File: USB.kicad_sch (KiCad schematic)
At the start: 44 parts, among them J2 24FLZ-SM2-TB, J5 DM3BT-DSF-PEJS, M1 IMP34DT05TR, M2 IMP34DT05TR, Q1 AO3401A, U3 FDS9926A

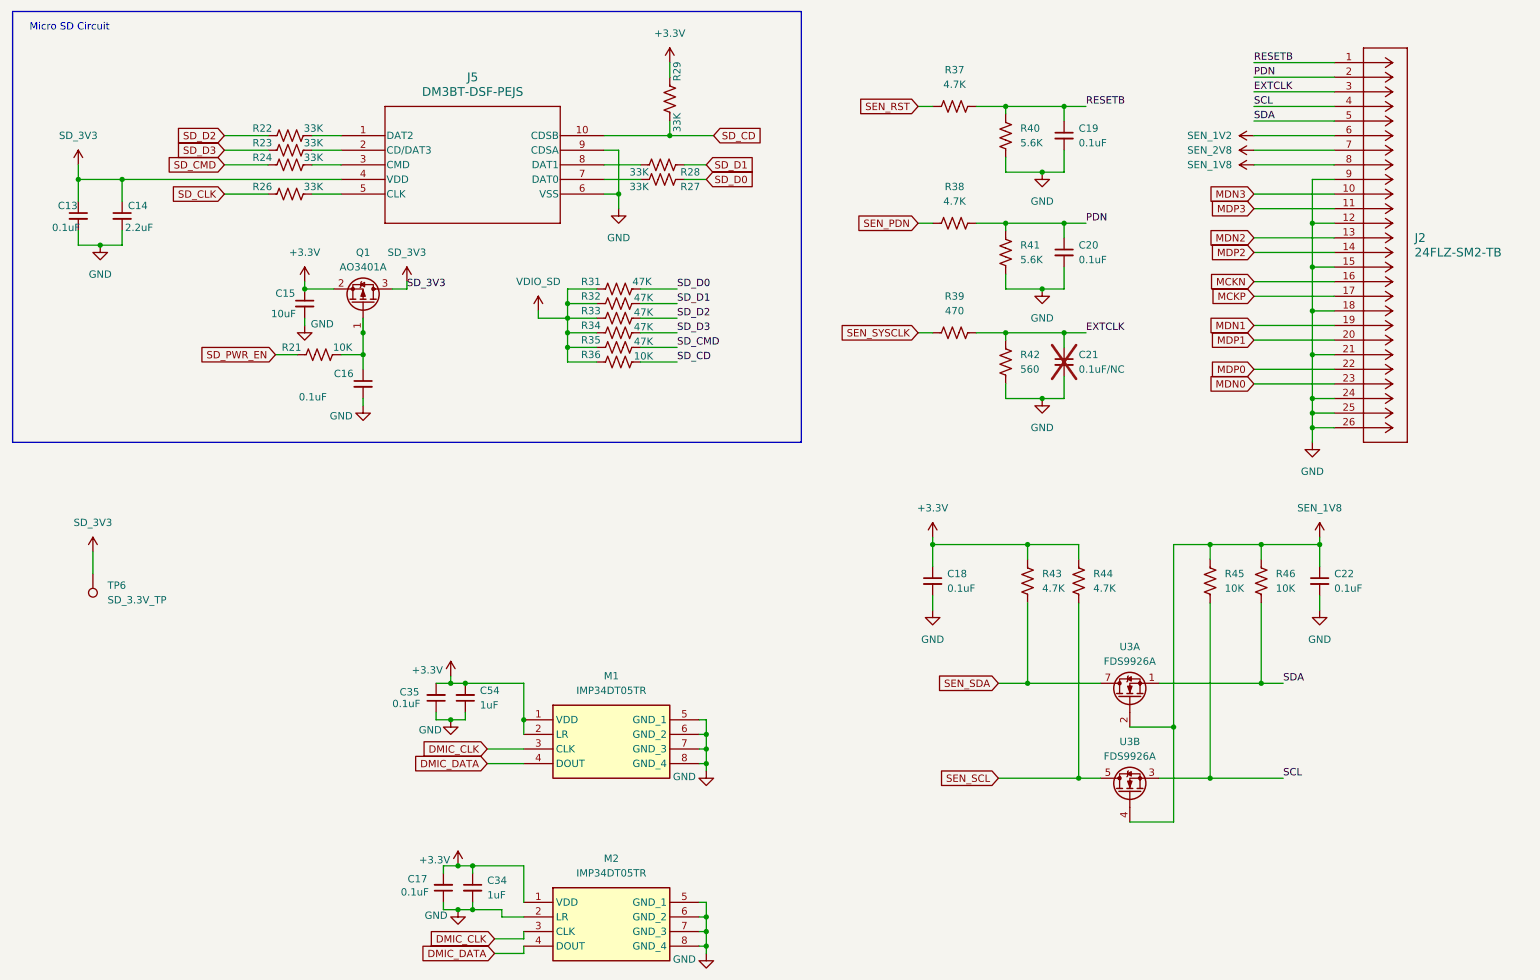
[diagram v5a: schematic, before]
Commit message: Replaced all passive footprints from 0603 metric to 0603 imperial. Big oversight. All done. Next is DRC
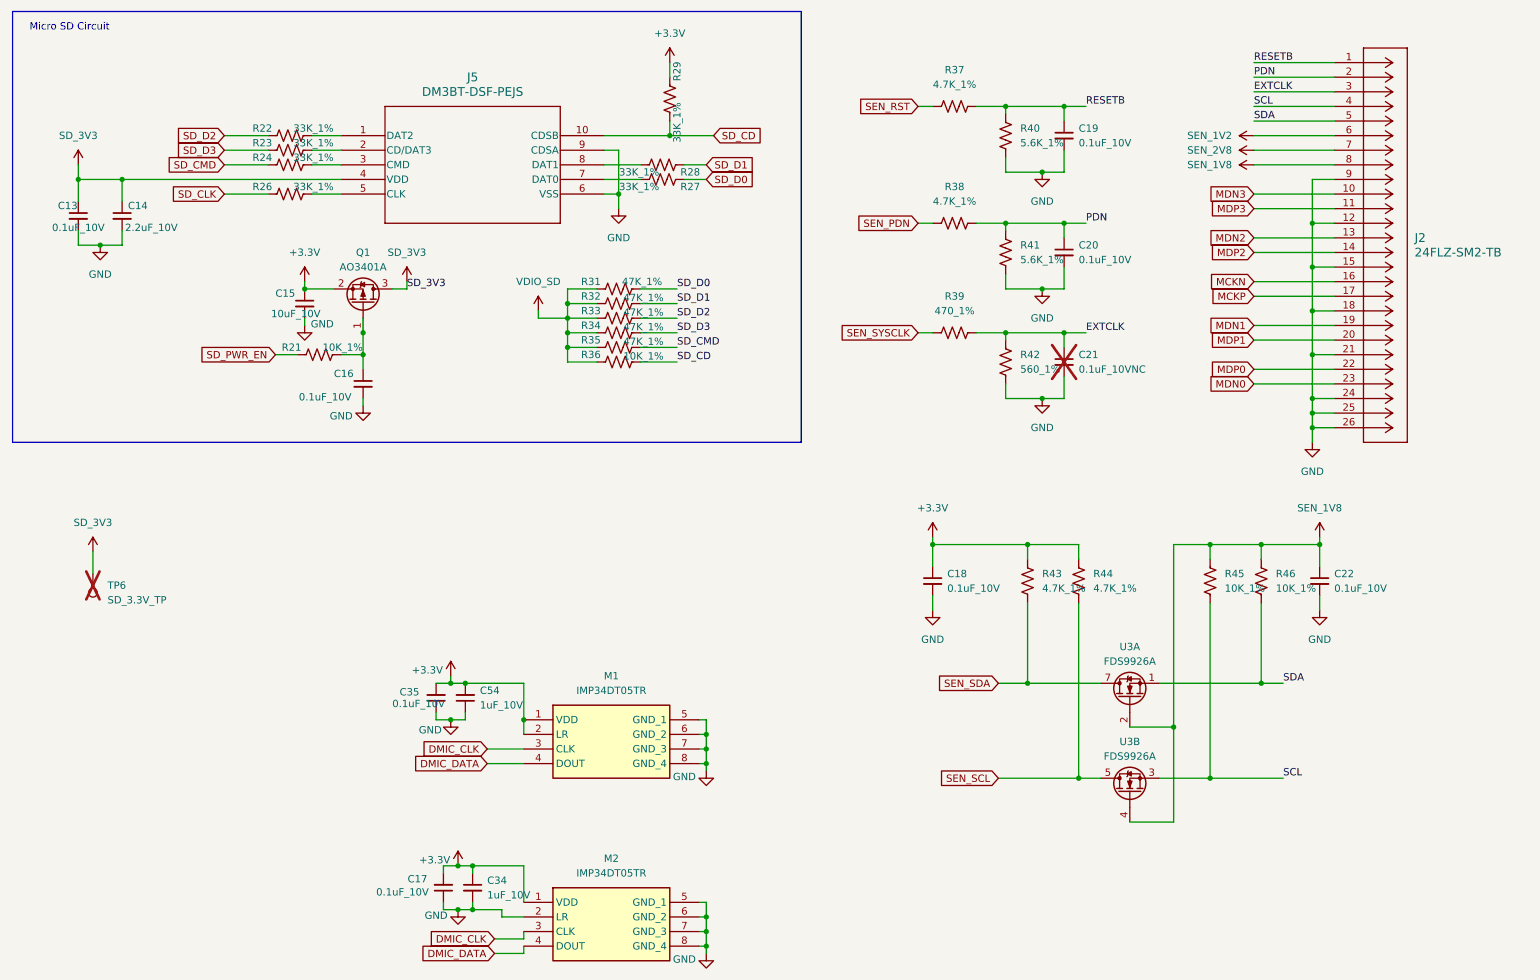
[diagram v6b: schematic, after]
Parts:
- C13, C16, C17, C18, C19, C20, C22, C35: value 0.1uF -> 0.1uF_10V; footprint Capacitor_SMD:C_0201_0603Metric_Pad0.64x0.40mm_HandSolder -> Capacitor_SMD:C_0603_1608Metric
- C14: value 2.2uF -> 2.2uF_10V; footprint Capacitor_SMD:C_0201_0603Metric_Pad0.64x0.40mm_HandSolder -> Capacitor_SMD:C_0603_1608Metric
- C15: value 10uF -> 10uF_10V; footprint Capacitor_SMD:C_0201_0603Metric_Pad0.64x0.40mm_HandSolder -> Capacitor_SMD:C_0603_1608Metric
- C21: value 0.1uF/NC -> 0.1uF_10VNC; footprint Capacitor_SMD:C_0201_0603Metric_Pad0.64x0.40mm_HandSolder -> Capacitor_SMD:C_0603_1608Metric
- C34, C54: value 1uF -> 1uF_10V; footprint Capacitor_SMD:C_0201_0603Metric_Pad0.64x0.40mm_HandSolder -> Capacitor_SMD:C_0603_1608Metric
- R21, R36, R45, R46: value 10K -> 10K_1%; footprint Resistor_SMD:R_0201_0603Metric_Pad0.64x0.40mm_HandSolder -> Resistor_SMD:R_0603_1608Metric
- R22, R23, R24, R26, R27, R28, R29: value 33K -> 33K_1%; footprint Resistor_SMD:R_0201_0603Metric_Pad0.64x0.40mm_HandSolder -> Resistor_SMD:R_0603_1608Metric
- R31, R32, R33, R34, R35: value 47K -> 47K_1%; footprint Resistor_SMD:R_0201_0603Metric_Pad0.64x0.40mm_HandSolder -> Resistor_SMD:R_0603_1608Metric
- R37, R38, R43, R44: value 4.7K -> 4.7K_1%; footprint Resistor_SMD:R_0201_0603Metric_Pad0.64x0.40mm_HandSolder -> Resistor_SMD:R_0603_1608Metric
- R39: value 470 -> 470_1%; footprint Resistor_SMD:R_0201_0603Metric_Pad0.64x0.40mm_HandSolder -> Resistor_SMD:R_0603_1608Metric
- R40, R41: value 5.6K -> 5.6K_1%; footprint Resistor_SMD:R_0201_0603Metric_Pad0.64x0.40mm_HandSolder -> Resistor_SMD:R_0603_1608Metric
- R42: value 560 -> 560_1%; footprint Resistor_SMD:R_0201_0603Metric_Pad0.64x0.40mm_HandSolder -> Resistor_SMD:R_0603_1608Metric
- TP6: now not fitted

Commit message: All fiducials and mounting holes placed. Except one hole, which I'll try to place. WIP
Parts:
- J2: footprint CON24_1X24_DB_JST -> JST 24FLZ-SM2-TB:CON24_1X24_DB_JST
- J5: footprint DM3BT-DSF-PEJS_HIR -> DM3BT-DSF-PEJS:DM3BT-DSF-PEJS_HIR
- M1, M2: footprint IMP34DT05TR -> IMP34DT05TR:IMP34DT05TR
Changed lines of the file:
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@@
 			)
 		)
-		(property "Footprint" "DM3BT-DSF-PEJS_HIR"
+		(property "Footprint" "DM3BT-DSF-PEJS:DM3BT-DSF-PEJS_HIR"
 			(at 74.93 39.37 0)
 			(effects
@@
 			)
 		)
-		(property "Footprint" "IMP34DT05TR"
+		(property "Footprint" "IMP34DT05TR:IMP34DT05TR"
 			(at 133.35 267.64 0)
 			(effects
@@
 			)
 		)
-		(property "Footprint" "IMP34DT05TR"
+		(property "Footprint" "IMP34DT05TR:IMP34DT05TR"
 			(at 133.35 235.89 0)
 			(effects
@@
 			)
 		)
-		(property "Footprint" "CON24_1X24_DB_JST"
+		(property "Footprint" "JST 24FLZ-SM2-TB:CON24_1X24_DB_JST"
 			(at 247.65 26.67 0)
 			(effects
